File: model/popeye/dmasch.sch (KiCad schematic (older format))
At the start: 26 parts, among them U1 74LS04, U1B1 74LS00, U1D1 74LS00, U1E1 74LS138, U1F1 74LS161, U1L1 74LS74, U2 74LS74, U2D1 74LS74, U2E1 74LS161, U2F1 74LS161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

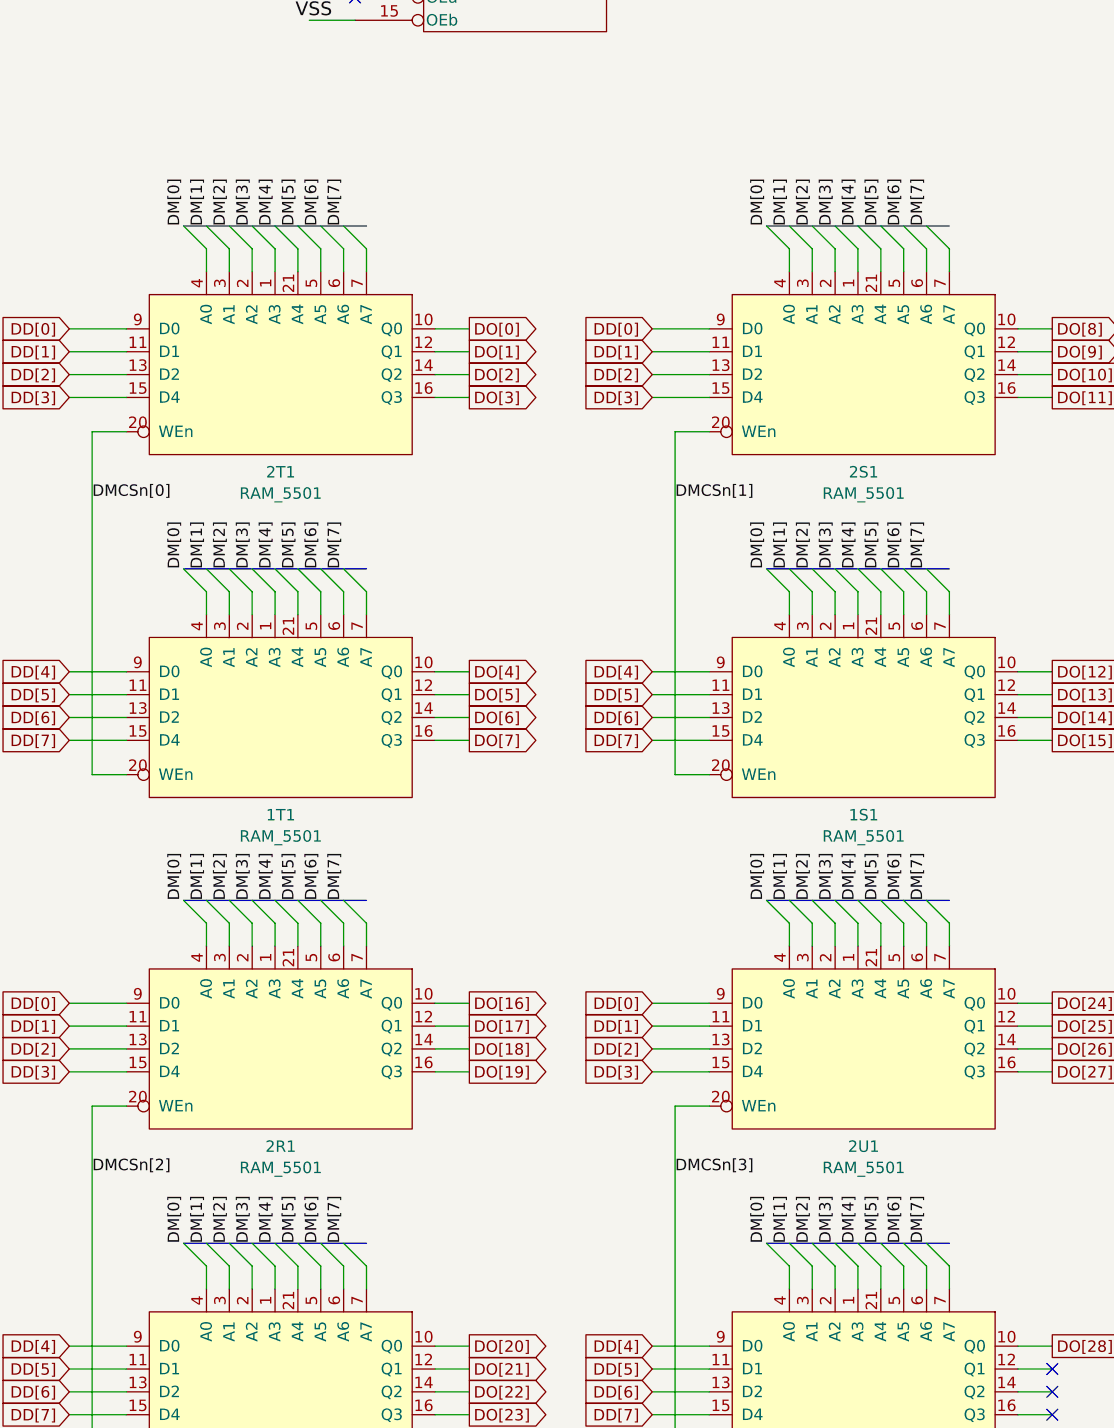
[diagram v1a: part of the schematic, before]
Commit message: Fixed background upside down problem
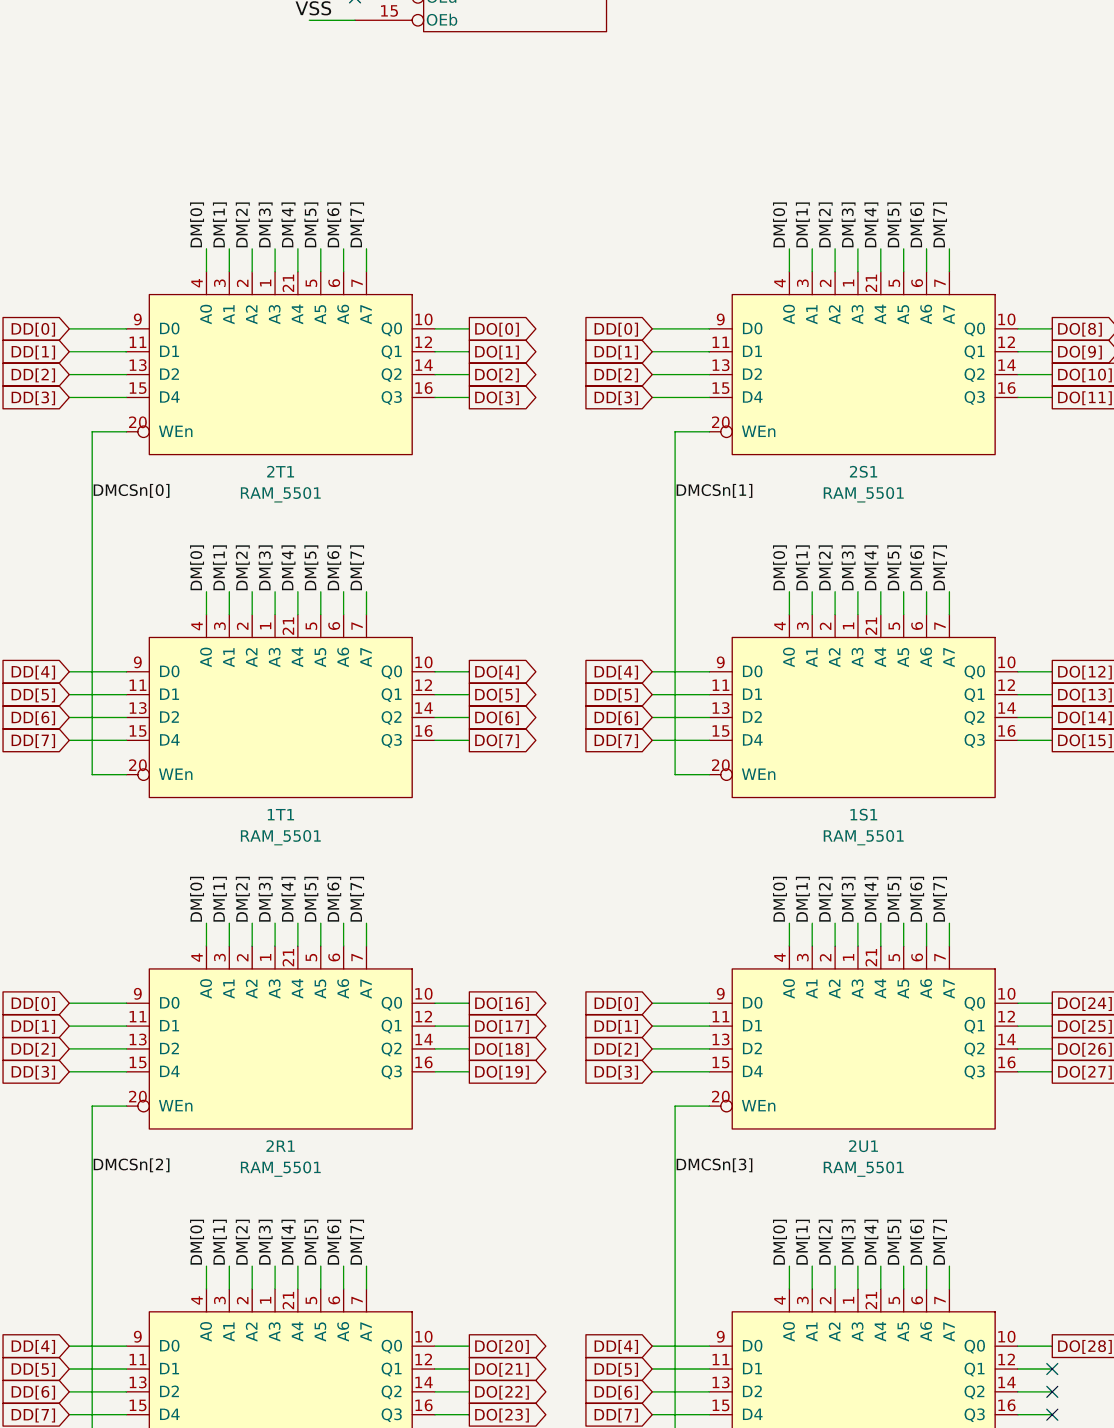
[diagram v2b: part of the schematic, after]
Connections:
- net DM[0]: now also 1R1.4 (A0), 1S1.4 (A0), 1T1.4 (A0), 1U1.4 (A0), 2R1.4 (A0), 2S1.4 (A0), 2T1.4 (A0), 2U1.4 (A0)
- net DM[1]: now also 1R1.3 (A1), 1S1.3 (A1), 1T1.3 (A1), 1U1.3 (A1), 2R1.3 (A1), 2S1.3 (A1), 2T1.3 (A1), 2U1.3 (A1)
- net DM[2]: now also 1R1.2 (A2), 1S1.2 (A2), 1T1.2 (A2), 1U1.2 (A2), 2R1.2 (A2), 2S1.2 (A2), 2T1.2 (A2), 2U1.2 (A2)
- net DM[3]: now also 1R1.1 (A3), 1S1.1 (A3), 1T1.1 (A3), 1U1.1 (A3), 2R1.1 (A3), 2S1.1 (A3), 2T1.1 (A3), 2U1.1 (A3)
- net DM[4]: now also 1R1.21 (A4), 1S1.21 (A4), 1T1.21 (A4), 1U1.21 (A4), 2R1.21 (A4), 2S1.21 (A4), 2T1.21 (A4), 2U1.21 (A4)
- net DM[5]: now also 1R1.5 (A5), 1S1.5 (A5), 1T1.5 (A5), 1U1.5 (A5), 2R1.5 (A5), 2S1.5 (A5), 2T1.5 (A5), 2U1.5 (A5)
- net DM[6]: now also 1R1.6 (A6), 1S1.6 (A6), 1T1.6 (A6), 1U1.6 (A6), 2R1.6 (A6), 2S1.6 (A6), 2T1.6 (A6), 2U1.6 (A6)
- net DM[7]: now also 1R1.7 (A7), 1S1.7 (A7), 1T1.7 (A7), 1U1.7 (A7), 2R1.7 (A7), 2S1.7 (A7), 2T1.7 (A7), 2U1.7 (A7)
